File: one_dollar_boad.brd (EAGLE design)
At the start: 85.6 x 54 mm, 37 parts, among them IC1 ATTINY85, X1 USBPCB

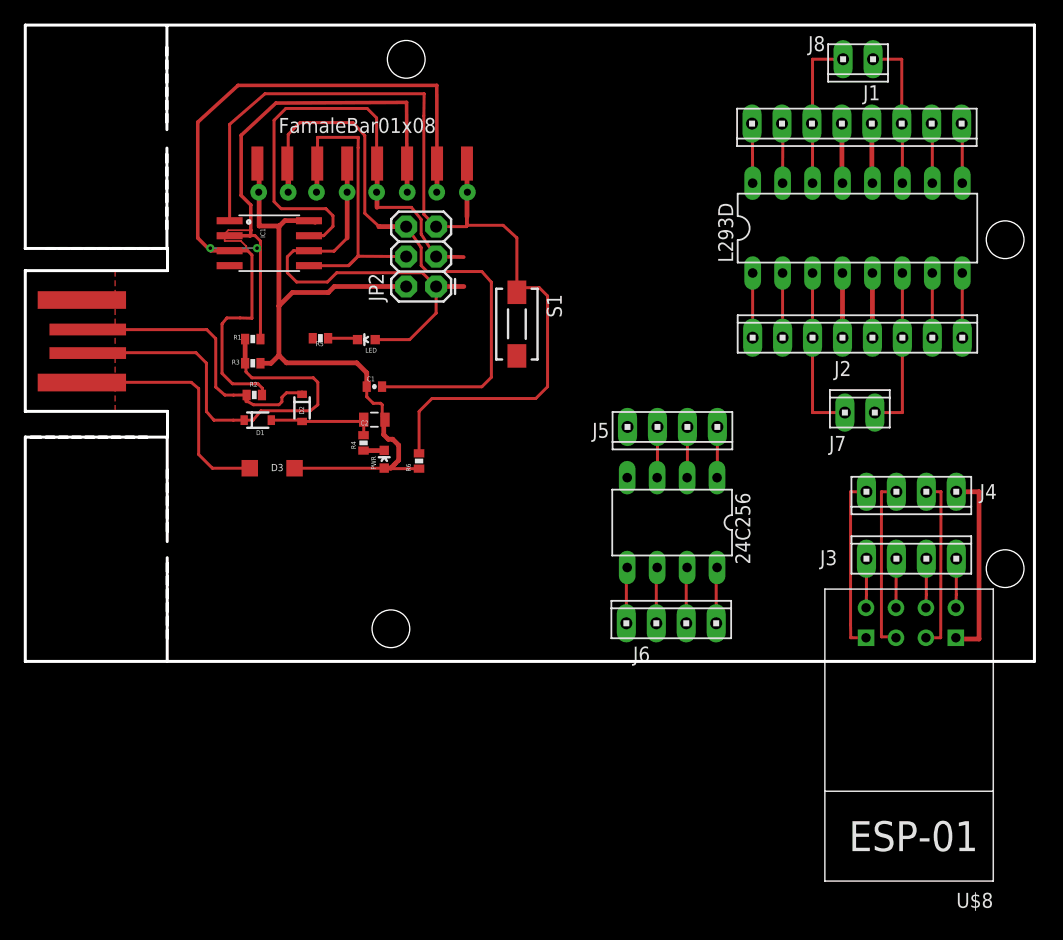
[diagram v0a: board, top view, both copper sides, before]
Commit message: `
- Adicionado slot para LD1117
- Adicionado Silk
- Cantos chanfrados
- Retirado GND dos componentes de expansão para que o usuário possa usar os expansores que achar melhor.
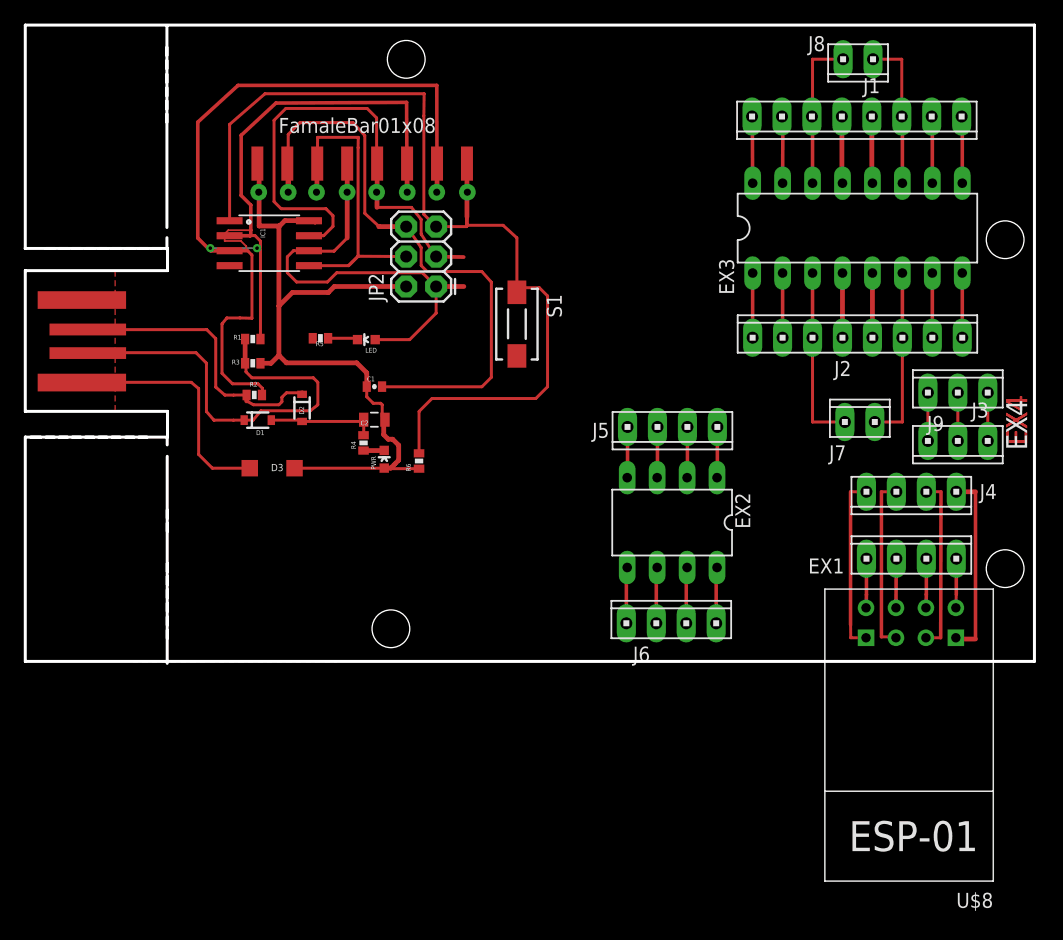
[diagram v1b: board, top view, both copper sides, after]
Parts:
- added EX1: (no value), con-amp:10X04MTA
- added J9: (no value), con-amp:10X03MTA
- J3: device con-amp:10X04MTA -> con-amp:10X03MTA
- moved J3 10.7 mm to (79.1, 18.7), turned to 180 degrees
- moved J7 0.80 mm to (70.8, 20.3)
- moved J1 0.60 mm to (70.5, 46.2)
- renumbered 24C256 to EX2, L293D to EX3
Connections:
- new net N$46: J4.4, U$8.GND
- new net N$47: EX2.4, J5.1
- new net N$48: EX3.5, J2.4
- new net N$49: EX3.12, J1.5
- new net N$50: EX3.13, J1.4
- new net N$51: EX3.4, J2.5
- new net N$52: J3.1, J9.3
- new net N$53: J3.2, J9.2
- new net N$54: J3.3, J9.1
- net GND: no longer EX2.4, EX3.12, EX3.13, EX3.4, EX3.5, J1.4, J1.5, J2.4, J2.5, J4.4, U$8.GND
- net N$32: now also EX1.1; no longer J3.1
- net N$33: now also EX1.2; no longer J3.2
- net N$34: now also EX1.3; no longer J3.3
- net N$35: now also EX1.4; no longer J3.4
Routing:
- net GND: track 103.2 -> 65.5 mm
- net N$46: track 0.00 -> 15.9 mm
- net N$50: track 0.00 -> 5.71 mm
- net N$49: track 0.00 -> 5.71 mm
- net N$51: track 0.00 -> 5.49 mm
- net N$48: track 0.00 -> 5.49 mm
- net N$47: track 0.00 -> 4.33 mm
- net N$54: track 0.00 -> 4.10 mm
- net N$53: track 0.00 -> 4.10 mm
- net N$52: track 0.00 -> 4.10 mm
- net N$25: track 13.2 -> 14.3 mm
- net N$20: track 14.2 -> 15.0 mm
- net N$15: track 14.6 -> 15.4 mm
- net N$21: track 5.06 -> 5.66 mm
- net N$27: track 5.08 -> 5.66 mm
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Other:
- board size 85.6 x 54 mm -> 85.6 x 54.1 mm
- board text added: "EX4"
- board text removed: "Based on project by Erik Kettenbugr, Digistump LLC - digistump.com 2012, Modified by Thalis Antunes at the request of Claudio Olmedo"
- board text removed: "CH"
- board text removed: "GND"
- board text removed: "GP0"
- board text removed: "GP1"
- board text removed: "IN.A"
- board text removed: "IN.B"
- board text removed: "OUT.M1"
- board text removed: "OUT.M2"
- board text removed: "PWM"
- board text removed: "RST"
- board text removed: "RXD"
- board text removed: "VCC"
- board text removed: "VIN"

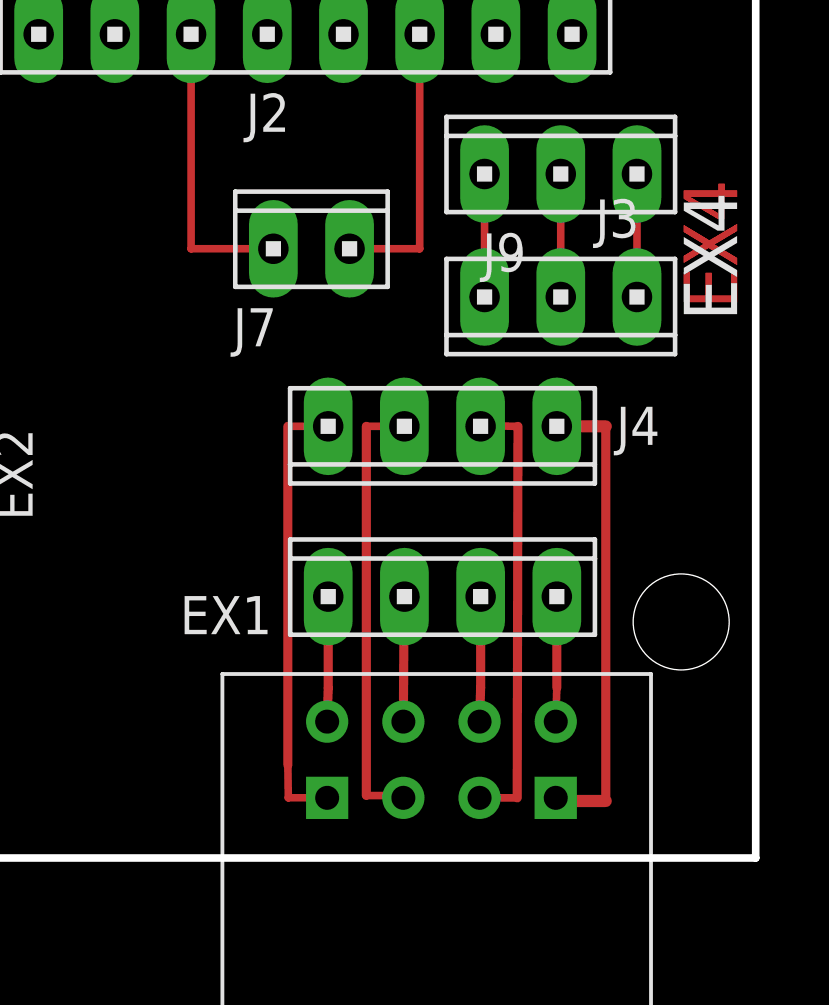
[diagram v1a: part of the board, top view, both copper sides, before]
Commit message: Pinos ESP8266
Adicionado numeração de identificação para os pinos do ESP8266
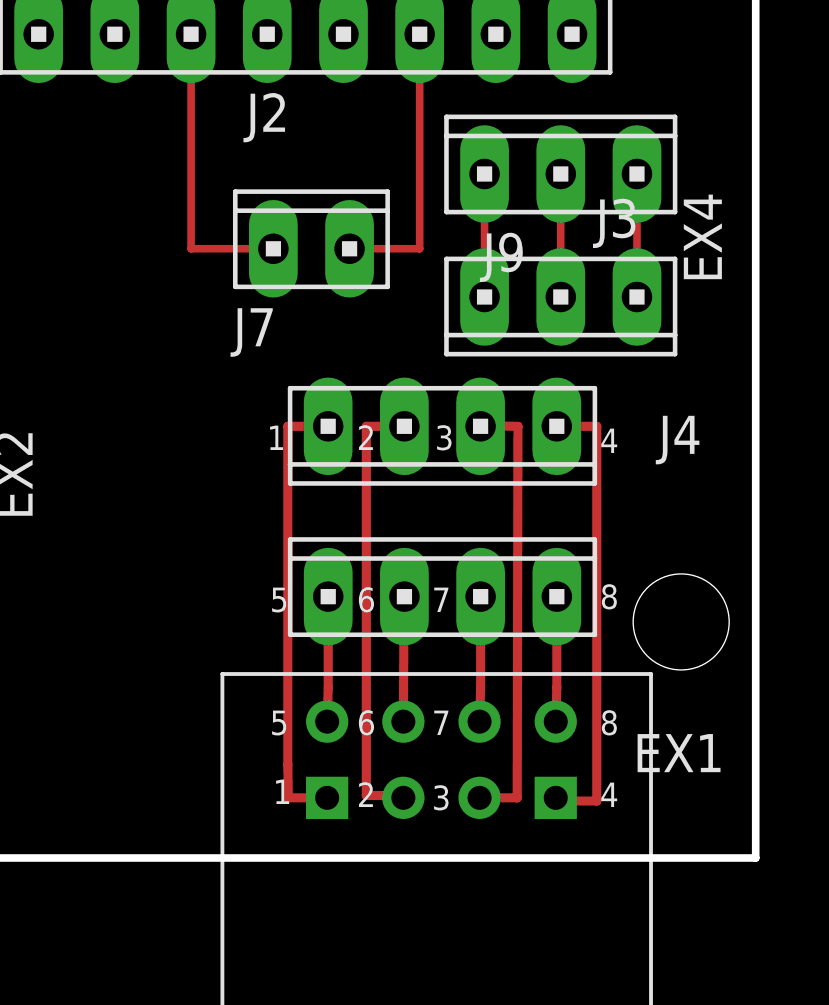
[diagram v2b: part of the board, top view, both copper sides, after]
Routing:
- net N$46: track 15.9 -> 15.3 mm
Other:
- board text added: "1"
- board text added: "2"
- board text added: "3"
- board text added: "4"
- board text added: "5"
- board text added: "6"
- board text added: "7"
- board text added: "8"
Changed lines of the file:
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@@
 <wire x1="85.6" y1="1.8" x2="83.8" y2="0" width="0.254" layer="44" curve="-90"/>
 <wire x1="83.8" y1="0" x2="83.7" y2="0" width="0.254" layer="44"/>
-<text x="83.2" y="22.6" size="1.778" layer="1" rot="R270">EX4</text>
-<text x="83.2" y="22.6" size="1.778" layer="1" rot="R270">EX4</text>
-<text x="83.2" y="22.2" size="1.778" layer="21" rot="R270">EX4</text>
+<text x="83.2" y="22.2" size="1.27" layer="21" rot="R270">EX4</text>
+<text x="69.3" y="13.6" size="0.8128" layer="21">1</text>
+<text x="69.5" y="1.8" size="0.8128" layer="21">1</text>
+<text x="72.3" y="13.6" size="0.8128" layer="21">2</text>
+<text x="74.9" y="13.6" size="0.8128" layer="21">3</text>
+<text x="80.4" y="13.5" size="0.8128" layer="21">4</text>
+<text x="72.3" y="1.7" size="0.8128" layer="21">2</text>
+<text x="74.8" y="1.6" size="0.8128" layer="21">3</text>
+<text x="80.4" y="1.7" size="0.8128" layer="21">4</text>
+<text x="69.4" y="4.1" size="0.8128" layer="21">5</text>
+<text x="72.3" y="4.1" size="0.8128" layer="21">6</text>
+<text x="74.8" y="4.1" size="0.8128" layer="21">7</text>
+<text x="80.4" y="4.1" size="0.8128" layer="21">8</text>
+<text x="69.4" y="8.2" size="0.8128" layer="21">5</text>
+<text x="80.4" y="8.3" size="0.8128" layer="21">8</text>
+<text x="72.3" y="8.2" size="0.8128" layer="21">6</text>
+<text x="74.8" y="8.2" size="0.8128" layer="21">7</text>
 </plain>
 <attributes>
@@
 <element name="U$8" library="esp8266modules" package="ESP01" value="ESP01" x="75.1078" y="-3.6322" rot="R180"/>
 <element name="EX1" library="con-amp" package="10X04MTA" value="" x="75.1586" y="8.7122" smashed="yes">
-<attribute name="NAME" x="66.4074" y="7.461" size="1.27" layer="25"/>
+<attribute name="NAME" x="81.5074" y="2.861" size="1.27" layer="25"/>
 <attribute name="VALUE" x="70.1825" y="10.8631" size="1.27" layer="27"/>
 </element>
 <element name="J4" library="con-amp" package="10X04MTA" value="" x="75.157" y="14.3892" smashed="yes" rot="R180">
-<attribute name="NAME" x="82.4082" y="15.0404" size="1.27" layer="25" rot="R180"/>
+<attribute name="NAME" x="83.8082" y="14.7404" size="1.27" layer="25" rot="R180"/>
 <attribute name="VALUE" x="80.1331" y="12.2383" size="1.27" layer="27" rot="R180"/>
 </element>
@@
 <contactref element="U$8" pad="GPIO2"/>
 <contactref element="J4" pad="3"/>
-<wire x1="76.3928" y1="2.0053" x2="77.6478" y2="2.0053" width="0.254" layer="1"/>
+<wire x1="76.3928" y1="2.0053" x2="77.6478" y2="2.0053" width="0.3048" layer="1"/>
 <wire x1="77.6478" y1="2.0053" x2="77.6732" y2="14.3876" width="0.3048" layer="1"/>
-<wire x1="77.6732" y1="14.3876" x2="76.4524" y2="14.413" width="0.254" layer="1"/>
+<wire x1="77.6732" y1="14.3876" x2="76.4524" y2="14.413" width="0.3048" layer="1"/>
 <wire x1="76.4524" y1="14.413" x2="76.427" y2="14.3892" width="0.254" layer="1"/>
 </signal>
@@
 <contactref element="U$8" pad="GPIO0"/>
 <contactref element="J4" pad="2"/>
-<wire x1="73.887" y1="14.3892" x2="72.6186" y2="14.3892" width="0.254" layer="1"/>
+<wire x1="73.887" y1="14.3892" x2="72.6186" y2="14.3892" width="0.3048" layer="1"/>
 <wire x1="72.6186" y1="14.3892" x2="72.6186" y2="2.0828" width="0.3048" layer="1"/>
-<wire x1="72.6186" y1="2.0828" x2="73.8782" y2="2.0828" width="0.254" layer="1"/>
+<wire x1="72.6186" y1="2.0828" x2="73.8782" y2="2.0828" width="0.3048" layer="1"/>
 <wire x1="73.8782" y1="2.0828" x2="73.8528" y2="2.0053" width="0.254" layer="1"/>
 </signal>
@@
 <contactref element="U$8" pad="RX"/>
 <contactref element="J4" pad="1"/>
-<wire x1="71.347" y1="14.3892" x2="70.0024" y2="14.3892" width="0.254" layer="1"/>
+<wire x1="71.347" y1="14.3892" x2="70.0024" y2="14.3892" width="0.3048" layer="1"/>
 <wire x1="70.0024" y1="14.3892" x2="70.0024" y2="3.0988" width="0.3048" layer="1"/>
-<wire x1="70.0024" y1="3.0988" x2="70.0174" y2="2.0066" width="0.254" layer="1"/>
-<wire x1="70.0174" y1="2.0066" x2="71.3128" y2="2.0053" width="0.254" layer="1"/>
+<wire x1="70.0024" y1="3.0988" x2="70.0174" y2="2.0066" width="0.3048" layer="1"/>
+<wire x1="70.0174" y1="2.0066" x2="71.3128" y2="2.0053" width="0.3048" layer="1"/>
 </signal>
 <signal name="N$32">
@@
 <contactref element="EX1" pad="1"/>
 <wire x1="78.9686" y1="8.7122" x2="78.9686" y2="5.6779" width="0.3048" layer="1"/>
-<wire x1="78.9686" y1="5.6779" x2="78.9328" y2="4.5453" width="0.254" layer="1"/>
+<wire x1="78.9686" y1="5.6779" x2="78.9328" y2="4.5453" width="0.3048" layer="1"/>
 </signal>
 <signal name="N$33">
@@
 <contactref element="U$8" pad="GND"/>
 <contactref element="J4" pad="4"/>
-<wire x1="78.967" y1="14.3892" x2="80.6" y2="14.3892" width="0.4064" layer="1"/>
-<wire x1="80.6" y1="14.3892" x2="80.6" y2="1.9" width="0.3048" layer="1"/>
-<wire x1="80.6" y1="1.9" x2="78.9328" y2="1.9" width="0.4064" layer="1"/>
+<wire x1="78.967" y1="14.3892" x2="80.3" y2="14.3892" width="0.3048" layer="1"/>
+<wire x1="80.3" y1="14.3892" x2="80.3" y2="1.9" width="0.3048" layer="1"/>
+<wire x1="80.3" y1="1.9" x2="78.9328" y2="1.9" width="0.3048" layer="1"/>
 <wire x1="78.9328" y1="1.9" x2="78.9328" y2="2.0053" width="0.4064" layer="1"/>
 </signal>

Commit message: Pinos ESP8266
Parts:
- moved J3 1.02 mm to (79.3, 19.7)
- moved J9 1.02 mm to (79.3, 23.8)
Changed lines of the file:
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@@
 <wire x1="85.6" y1="1.8" x2="83.8" y2="0" width="0.254" layer="44" curve="-90"/>
 <wire x1="83.8" y1="0" x2="83.7" y2="0" width="0.254" layer="44"/>
-<text x="83.2" y="22.2" size="1.27" layer="21" rot="R270">EX4</text>
-<text x="69.3" y="13.6" size="0.8128" layer="21">1</text>
-<text x="69.5" y="1.8" size="0.8128" layer="21">1</text>
-<text x="72.3" y="13.6" size="0.8128" layer="21">2</text>
-<text x="74.9" y="13.6" size="0.8128" layer="21">3</text>
-<text x="80.4" y="13.5" size="0.8128" layer="21">4</text>
-<text x="72.3" y="1.7" size="0.8128" layer="21">2</text>
-<text x="74.8" y="1.6" size="0.8128" layer="21">3</text>
-<text x="80.4" y="1.7" size="0.8128" layer="21">4</text>
-<text x="69.4" y="4.1" size="0.8128" layer="21">5</text>
-<text x="72.3" y="4.1" size="0.8128" layer="21">6</text>
-<text x="74.8" y="4.1" size="0.8128" layer="21">7</text>
-<text x="80.4" y="4.1" size="0.8128" layer="21">8</text>
-<text x="69.4" y="8.2" size="0.8128" layer="21">5</text>
-<text x="80.4" y="8.3" size="0.8128" layer="21">8</text>
-<text x="72.3" y="8.2" size="0.8128" layer="21">6</text>
-<text x="74.8" y="8.2" size="0.8128" layer="21">7</text>
+<text x="83.4" y="23.2" size="1.27" layer="21" rot="R270">EX4</text>
+<text x="71" y="16.2" size="0.8128" layer="21">1</text>
+<text x="71" y="0.3" size="0.8128" layer="21">1</text>
+<text x="73.6" y="16.2" size="0.8128" layer="21">2</text>
+<text x="76" y="16.2" size="0.8128" layer="21">3</text>
+<text x="78.5" y="16.2" size="0.8128" layer="21">4</text>
+<text x="73.5" y="0.3" size="0.8128" layer="21">2</text>
+<text x="76.1" y="0.3" size="0.8128" layer="21">3</text>
+<text x="78.5" y="0.3" size="0.8128" layer="21">4</text>
+<text x="71" y="5.6" size="0.8128" layer="21">5</text>
+<text x="73.6" y="5.6" size="0.8128" layer="21">6</text>
+<text x="76.2" y="5.6" size="0.8128" layer="21">7</text>
+<text x="78.6" y="5.6" size="0.8128" layer="21">8</text>
+<text x="71.1" y="10.7" size="0.8128" layer="21">5</text>
+<text x="78.7" y="10.7" size="0.8128" layer="21">8</text>
+<text x="73.6" y="10.7" size="0.8128" layer="21">6</text>
+<text x="76.1" y="10.7" size="0.8128" layer="21">7</text>
 </plain>
 <attributes>
@@
 <element name="ICSP6" library="ICSP" package="ICSP" value="ICSP" x="30" y="31.8"/>
 <element name="R6" library="SparkFun-Passives" package="0402-RES" value="" x="33.4" y="17" rot="R90"/>
-<element name="J3" library="con-amp" package="10X03MTA" value="" x="79.1" y="18.7" rot="R180"/>
-<element name="J9" library="con-amp" package="10X03MTA" value="" x="79.1" y="22.8"/>
+<element name="J3" library="con-amp" package="10X03MTA" value="" x="79.3" y="19.7" rot="R180"/>
+<element name="J9" library="con-amp" package="10X03MTA" value="" x="79.3" y="23.8"/>
 </elements>
 <signals>
@@
 <contactref element="J9" pad="3"/>
 <contactref element="J3" pad="1"/>
-<wire x1="76.56" y1="18.7" x2="76.56" y2="22.8" width="0.254" layer="1"/>
+<wire x1="76.76" y1="19.7" x2="76.76" y2="23.8" width="0.254" layer="1"/>
 </signal>
 <signal name="N$53">
 <contactref element="J3" pad="2"/>
 <contactref element="J9" pad="2"/>
-<wire x1="79.1" y1="18.7" x2="79.1" y2="22.8" width="0.254" layer="1"/>
+<wire x1="79.3" y1="19.7" x2="79.3" y2="23.8" width="0.254" layer="1"/>
 </signal>
 <signal name="N$54">
 <contactref element="J9" pad="1"/>
 <contactref element="J3" pad="3"/>
-<wire x1="81.64" y1="18.7" x2="81.64" y2="22.8" width="0.254" layer="1"/>
+<wire x1="81.84" y1="19.7" x2="81.84" y2="23.8" width="0.254" layer="1"/>
 </signal>
 </signals>
